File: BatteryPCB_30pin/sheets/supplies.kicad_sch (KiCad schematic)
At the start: 6 parts, among them J5 to COTS altimeter, J6 to SRAD flight computer, SW2 COTS ARM, SW3 SRAD ARM

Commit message: Battery PCB 30-pin: test-point block on the right edge (5V, GND, COTS +/-, SRAD +/-)
Six through-hole test points together on the front right edge, between
the right rod's washer keep-out and the lower zip-tie cut-out, labelled
on the silk: top row TP1 +5V, TP5 COTS +, TP7 SRAD +; bottom row TP3 GND,
TP6 COTS -, TP8 SRAD -.

- TP1/TP3 moved out of the BT3/BT4 gap (hard to reach with cells in).
- TP5-TP8 are new (schematic sheet 4): the COTS and SRAD cells are
  isolated from GND, so each gets its own + / - pair, before the pin
  switch, so they read the cell whether armed or not.
- Routing: +5V from J1-15 (front, via at (44, 2), back); COTS/SRAD +
  from the top tabs down a channel beside BT4; COTS - (front) and
  SRAD - (back) from the bottom tabs under the zip-tie cut-out. Battery
  traces 1.0 mm (Pyro rules), +5V 0.8 mm.
- GND stitching: 3 vias removed where the block sits, 4 nudged <= 0.7 mm
  for clearance. Old TP1 feed removed; 'for zipties' label moved.
- verify_A checks all eight test points; README, layout notes and the
  order package's assembly scope updated; Gerbers, PDF, project zip and
  STEP regenerated. BOM and JLC files unchanged (test points are pads).

ERC 0 errors, DRC 0 (schematic parity, zones refilled, same 3
documented exclusions). No other part, trace or dimension changed.

Co-Authored-By: Claude Opus 5.5 <noreply@anthropic.com>
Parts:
- added TP5: TP_COTS+, TestPoint:TestPoint_THTPad_D2.0mm_Drill1.0mm, symbol Connector:TestPoint
- added TP6: TP_COTS-, TestPoint:TestPoint_THTPad_D2.0mm_Drill1.0mm, symbol Connector:TestPoint
- added TP7: TP_SRAD+, TestPoint:TestPoint_THTPad_D2.0mm_Drill1.0mm, symbol Connector:TestPoint
- added TP8: TP_SRAD-, TestPoint:TestPoint_THTPad_D2.0mm_Drill1.0mm, symbol Connector:TestPoint
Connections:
- net COTS_BAT+: now also TP5.1
- net COTS_BAT-: now also TP6.1
- net SRAD_BAT+: now also TP7.1
- net SRAD_BAT-: now also TP8.1
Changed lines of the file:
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@@
 		)
 	)
+	(symbol
+		(lib_id "Connector:TestPoint")
+		(at 50.80 45.72 0)
+		(unit 1)
+		(exclude_from_sim no)
+		(in_bom no)
+		(on_board yes)
+		(dnp no)
+		(property "Reference" "TP5"
+			(at 53.34 40.64 0)
+			(effects (font (size 1.27 1.27)) (justify left))
+		)
+		(property "Value" "TP_COTS+"
+			(at 53.34 43.18 0)
+			(effects (font (size 1.27 1.27)) (justify left))
+		)
+		(property "Footprint" "TestPoint:TestPoint_THTPad_D2.0mm_Drill1.0mm"
+			(at 50.80 45.72 0)
+			(effects (font (size 1.27 1.27)) (hide yes))
+		)
+		(property "Datasheet" ""
+			(at 50.80 45.72 0)
+			(effects (font (size 1.27 1.27)) (hide yes))
+		)
+		(property "Description" "Bench test point"
+			(at 50.80 45.72 0)
+			(effects (font (size 1.27 1.27)) (hide yes))
+		)
+		(pin "1")
+		(instances
+			(project "battery_pcb_30pin"
+				(path "/19ef3a32-de7c-46ee-a850-2420f6d47f94/d30d38cc-20d9-4e05-9f85-c70abea8b778"
+					(reference "TP5")
+					(unit 1)
+				)
+			)
+		)
+	)
+	(wire
+		(pts (xy 50.80 45.72) (xy 50.80 50.80))
+		(stroke (width 0) (type default))
+	)
+	(label "COTS_BAT+"
+		(at 50.80 50.80 0)
+		(fields_autoplaced yes)
+		(effects (font (size 1.27 1.27)) (justify left bottom))
+	)
+	(symbol
+		(lib_id "Connector:TestPoint")
+		(at 66.04 45.72 0)
+		(unit 1)
+		(exclude_from_sim no)
+		(in_bom no)
+		(on_board yes)
+		(dnp no)
+		(property "Reference" "TP6"
+			(at 68.58 40.64 0)
+			(effects (font (size 1.27 1.27)) (justify left))
+		)
+		(property "Value" "TP_COTS-"
+			(at 68.58 43.18 0)
+			(effects (font (size 1.27 1.27)) (justify left))
+		)
+		(property "Footprint" "TestPoint:TestPoint_THTPad_D2.0mm_Drill1.0mm"
+			(at 66.04 45.72 0)
+			(effects (font (size 1.27 1.27)) (hide yes))
+		)
+		(property "Datasheet" ""
+			(at 66.04 45.72 0)
+			(effects (font (size 1.27 1.27)) (hide yes))
+		)
+		(property "Description" "Bench test point"
+			(at 66.04 45.72 0)
+			(effects (font (size 1.27 1.27)) (hide yes))
+		)
+		(pin "1")
+		(instances
+			(project "battery_pcb_30pin"
+				(path "/19ef3a32-de7c-46ee-a850-2420f6d47f94/d30d38cc-20d9-4e05-9f85-c70abea8b778"
+					(reference "TP6")
+					(unit 1)
+				)
+			)
+		)
+	)
+	(wire
+		(pts (xy 66.04 45.72) (xy 66.04 50.80))
+		(stroke (width 0) (type default))
+	)
+	(label "COTS_BAT-"
+		(at 66.04 50.80 0)
+		(fields_autoplaced yes)
+		(effects (font (size 1.27 1.27)) (justify left bottom))
+	)
+	(symbol
+		(lib_id "Connector:TestPoint")
+		(at 50.80 101.60 0)
+		(unit 1)
+		(exclude_from_sim no)
+		(in_bom no)
+		(on_board yes)
+		(dnp no)
+		(property "Reference" "TP7"
+			(at 53.34 96.52 0)
+			(effects (font (size 1.27 1.27)) (justify left))
+		)
+		(property "Value" "TP_SRAD+"
+			(at 53.34 99.06 0)
+			(effects (font (size 1.27 1.27)) (justify left))
+		)
+		(property "Footprint" "TestPoint:TestPoint_THTPad_D2.0mm_Drill1.0mm"
+			(at 50.80 101.60 0)
+			(effects (font (size 1.27 1.27)) (hide yes))
+		)
+		(property "Datasheet" ""
+			(at 50.80 101.60 0)
+			(effects (font (size 1.27 1.27)) (hide yes))
+		)
+		(property "Description" "Bench test point"
+			(at 50.80 101.60 0)
+			(effects (font (size 1.27 1.27)) (hide yes))
+		)
+		(pin "1")
+		(instances
+			(project "battery_pcb_30pin"
+				(path "/19ef3a32-de7c-46ee-a850-2420f6d47f94/d30d38cc-20d9-4e05-9f85-c70abea8b778"
+					(reference "TP7")
+					(unit 1)
+				)
+			)
+		)
+	)
+	(wire
+		(pts (xy 50.80 101.60) (xy 50.80 106.68))
+		(stroke (width 0) (type default))
+	)
+	(label "SRAD_BAT+"
+		(at 50.80 106.68 0)
+		(fields_autoplaced yes)
+		(effects (font (size 1.27 1.27)) (justify left bottom))
+	)
+	(symbol
+		(lib_id "Connector:TestPoint")
+		(at 66.04 101.60 0)
+		(unit 1)
+		(exclude_from_sim no)
+		(in_bom no)
+		(on_board yes)
+		(dnp no)
+		(property "Reference" "TP8"
+			(at 68.58 96.52 0)
+			(effects (font (size 1.27 1.27)) (justify left))
+		)
+		(property "Value" "TP_SRAD-"
+			(at 68.58 99.06 0)
+			(effects (font (size 1.27 1.27)) (justify left))
+		)
+		(property "Footprint" "TestPoint:TestPoint_THTPad_D2.0mm_Drill1.0mm"
+			(at 66.04 101.60 0)
+			(effects (font (size 1.27 1.27)) (hide yes))
+		)
+		(property "Datasheet" ""
+			(at 66.04 101.60 0)
+			(effects (font (size 1.27 1.27)) (hide yes))
+		)
+		(property "Description" "Bench test point"
+			(at 66.04 101.60 0)
+			(effects (font (size 1.27 1.27)) (hide yes))
+		)
+		(pin "1")
+		(instances
+			(project "battery_pcb_30pin"
+				(path "/19ef3a32-de7c-46ee-a850-2420f6d47f94/d30d38cc-20d9-4e05-9f85-c70abea8b778"
+					(reference "TP8")
+					(unit 1)
+				)
+			)
+		)
+	)
+	(wire
+		(pts (xy 66.04 101.60) (xy 66.04 106.68))
+		(stroke (width 0) (type default))
+	)
+	(label "SRAD_BAT-"
+		(at 66.04 106.68 0)
+		(fields_autoplaced yes)
+		(effects (font (size 1.27 1.27)) (justify left bottom))
+	)
 )

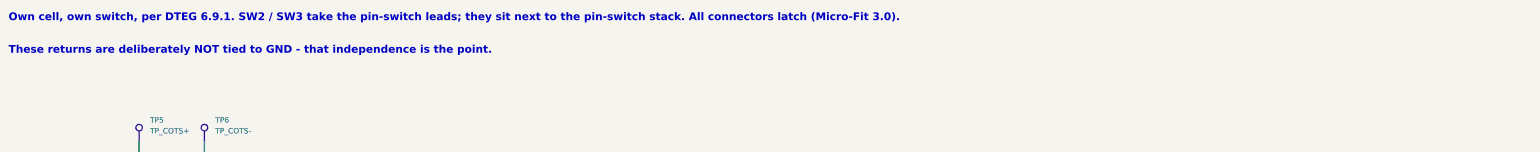
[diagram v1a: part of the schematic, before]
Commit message: Battery PCB 30-pin: XT30 and battery-holder holes to the datasheets; notes, check script
- XT30 J5/J6 pin holes 1.8 -> 1.9 mm (Amass drawing: 1.9 mm for the
  1.6 mm pins); 0.55 mm copper ring left on the 3.0 mm pads.
- Keystone 1042 holder peg holes 3.45 -> 3.5 mm and locator hole
  2.39 -> 2.4 mm on BT1-BT4 (Keystone M65p27; positions unchanged).
  Footprints updated in battery_pcb.pretty and on the board.
- Only those 16 hole sizes changed on the board: no part, trace, via,
  outline or silk moved. Tightest new gap: COTS_SW to a BT4 peg hole
  0.375 mm (rule 0.3).
- Schematic notes brought up to date: Q1 drop ~0.05 V (was 0.35 V from
  the old diode), J5/J6 are XT30 not Micro-Fit, C9/C10 sit at the
  ESP32's VIN (J1-15).
- verify_A: the old "seven edge cut-outs" count is replaced by a real
  check (7 rim notches + 4 square zip-tie cut-outs); ALL PASS, 36 checks.
- Gerbers, order-package zip, schematic PDF, project zip and STEP
  regenerated; BOM and CPL unchanged.

ERC 0 errors, DRC 0 (schematic parity, zones refilled, same 3
documented exclusions).

Co-Authored-By: Claude Opus 5.5 <noreply@anthropic.com>
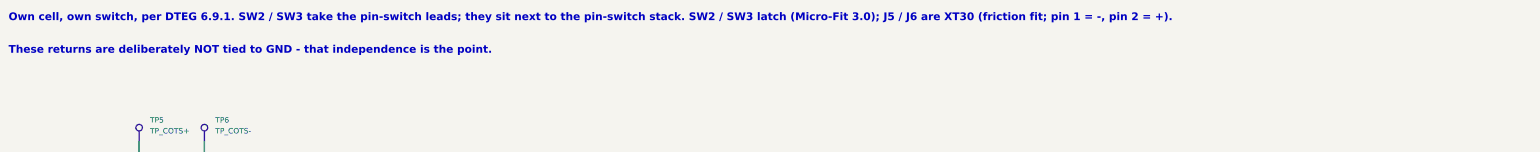
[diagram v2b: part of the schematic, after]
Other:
- note added: "Own cell, own switch, per DTEG 6.9.1. SW2 / SW3 take the pin-switch leads; they sit next to the pin-switch stack. SW2 / SW3 latch (Micro-Fit 3.0); J5 / J6 are XT30 (friction fit; pin 1 = -, pin 2 = +)."
- note removed: "Own cell, own switch, per DTEG 6.9.1. SW2 / SW3 take the pin-switch leads; they sit next to the pin-switch stack. All connectors latch (Micro-Fit 3.0)."
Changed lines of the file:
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@@
 		(company "Stanford SSI")
 	)
-	(text "Own cell, own switch, per DTEG 6.9.1. SW2 / SW3 take the pin-switch leads; they sit next to the pin-switch stack. All connectors latch (Micro-Fit 3.0)."
+	(text "Own cell, own switch, per DTEG 6.9.1. SW2 / SW3 take the pin-switch leads; they sit next to the pin-switch stack. SW2 / SW3 latch (Micro-Fit 3.0); J5 / J6 are XT30 (friction fit; pin 1 = -, pin 2 = +)."
 		(exclude_from_sim no)
 		(at 20.32 17.78 0)
